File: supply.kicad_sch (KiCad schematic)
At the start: 12 parts

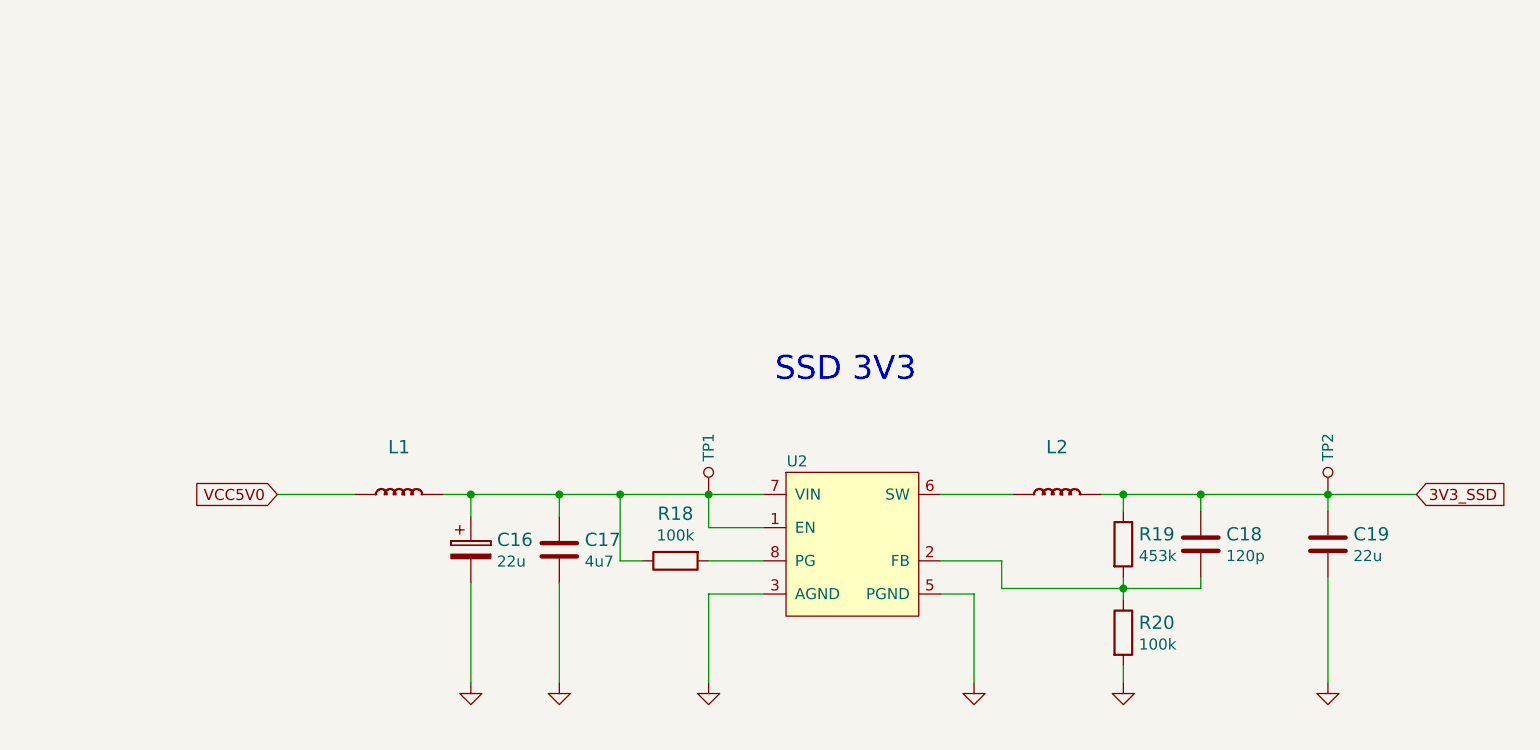
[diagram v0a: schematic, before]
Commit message: Exchanged flyback to CUI DCDC converter on schematics. Added logos.
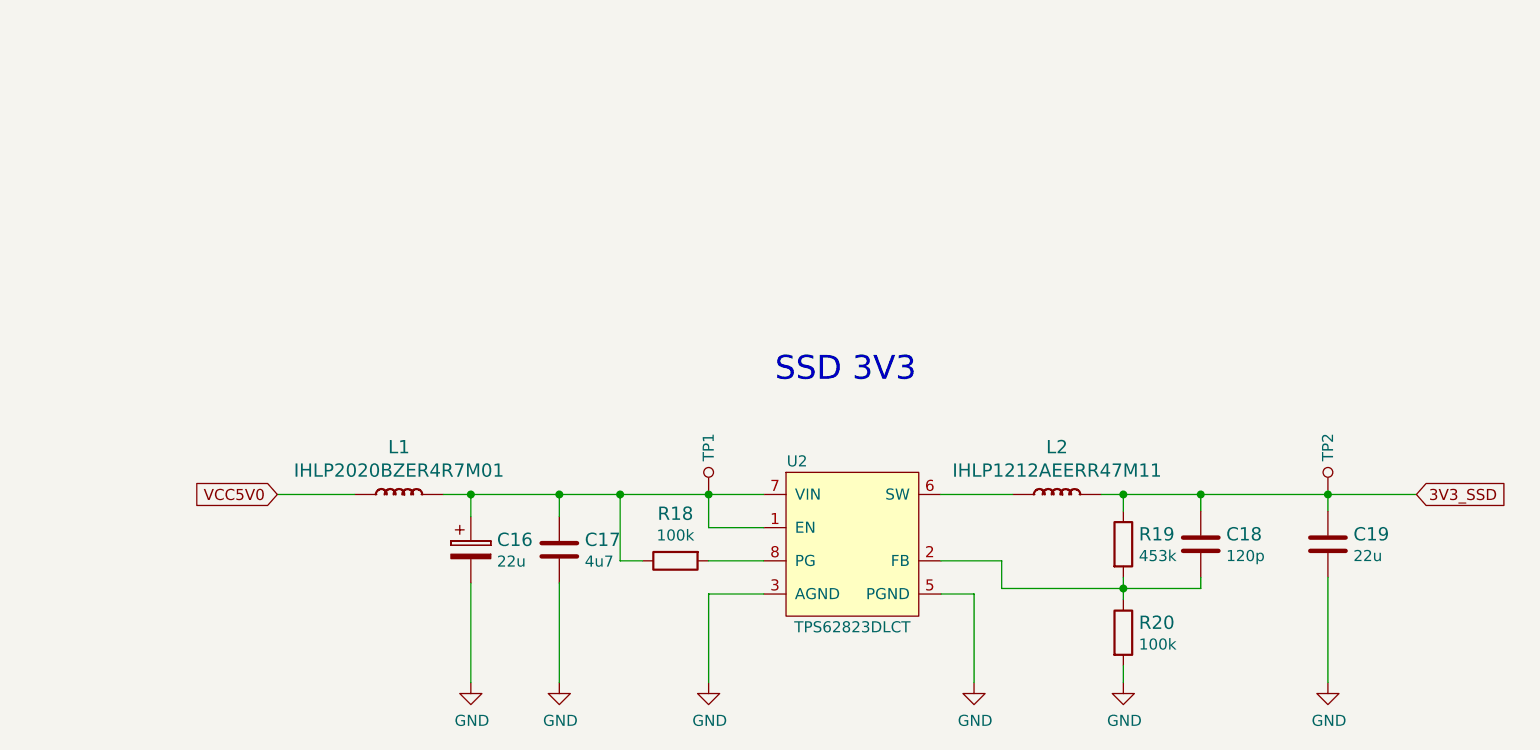
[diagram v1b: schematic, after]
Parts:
- C16: value (none) -> C_22u_KEMET_A; footprint scalenode-footprints: -> scalenode-footprints:KEMET_A
- C17: value (none) -> C_4u7_0603; footprint scalenode-footprints: -> scalenode-footprints:0603-cap
- C18: value (none) -> C_120p_0402; footprint scalenode-footprints: -> scalenode-footprints:0402-res
- C19: value (none) -> C_22u_1210; footprint scalenode-footprints: -> scalenode-footprints:1210-cap
- L1: value (none) -> IHLP2020BZER4R7M01; footprint scalenode-footprints: -> scalenode-footprints:IHLP2020BZER4R7M01
- L2: value (none) -> IHLP1212AEERR47M11; footprint scalenode-footprints: -> scalenode-footprints:IHLP-1212AE
- R18: value (none) -> R_100k_0603; footprint scalenode-footprints: -> scalenode-footprints:0603-res
- R19: value (none) -> R_453k_0402; footprint scalenode-footprints: -> scalenode-footprints:0402-res
- R20: value (none) -> R_100k_0402; footprint scalenode-footprints: -> scalenode-footprints:0402-res
- TP1, TP2: value (none) -> TP_SMD1MM; footprint scalenode-footprints: -> scalenode-footprints:Testpoint_smd_1mm
- U2: value (none) -> TPS62823DLCT; footprint scalenode-footprints: -> scalenode-footprints:QFN-8_2x1mm

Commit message: Added text fields with schematic descriptions
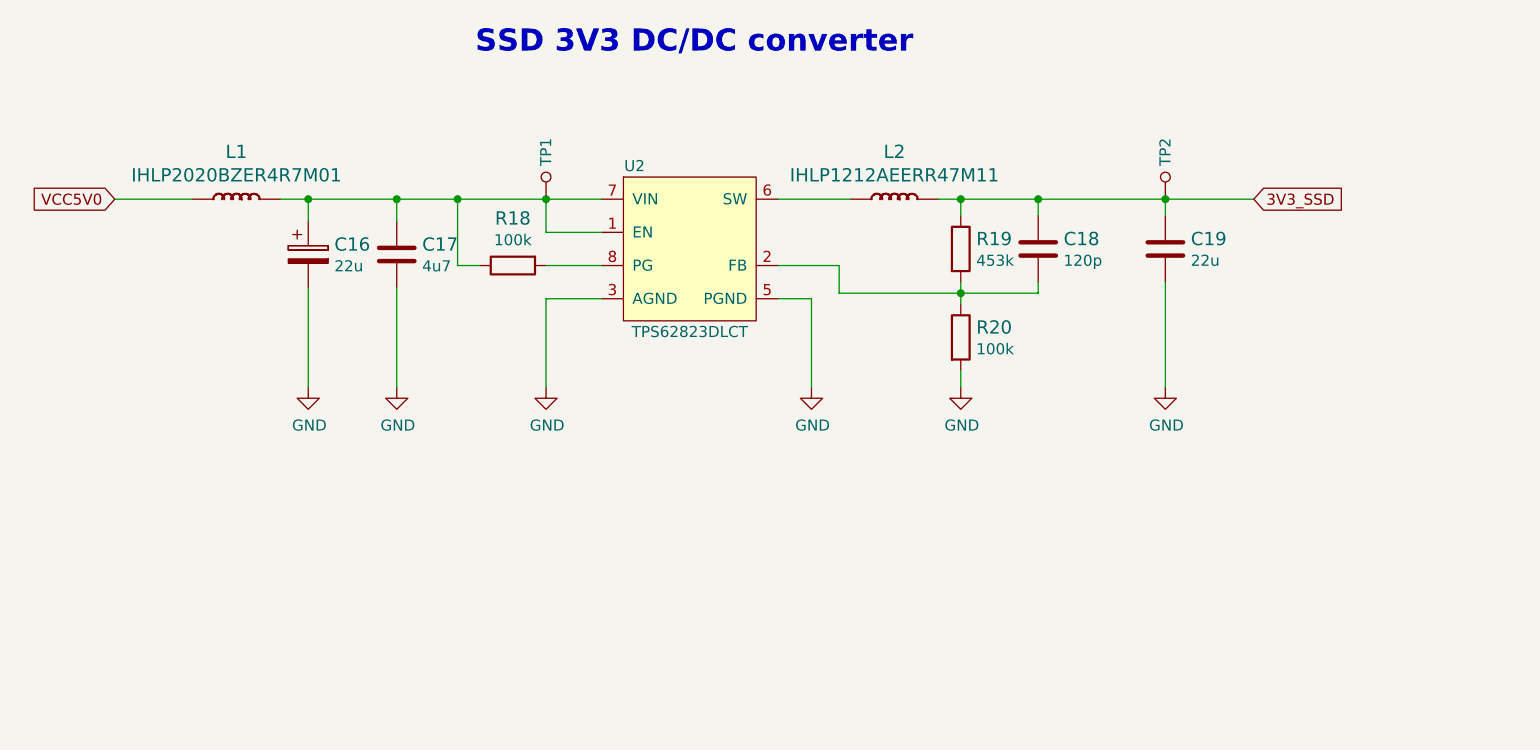
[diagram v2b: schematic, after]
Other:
- note added: "SSD 3V3 DC/DC converter"
- note removed: "SSD 3V3"
- moved on the sheet: C16, C17, C18, C19, L1, L2, R18, R19, R20, TP1, TP2, U2

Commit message: Implemented changes from rev 1.0.4. New components initial placement
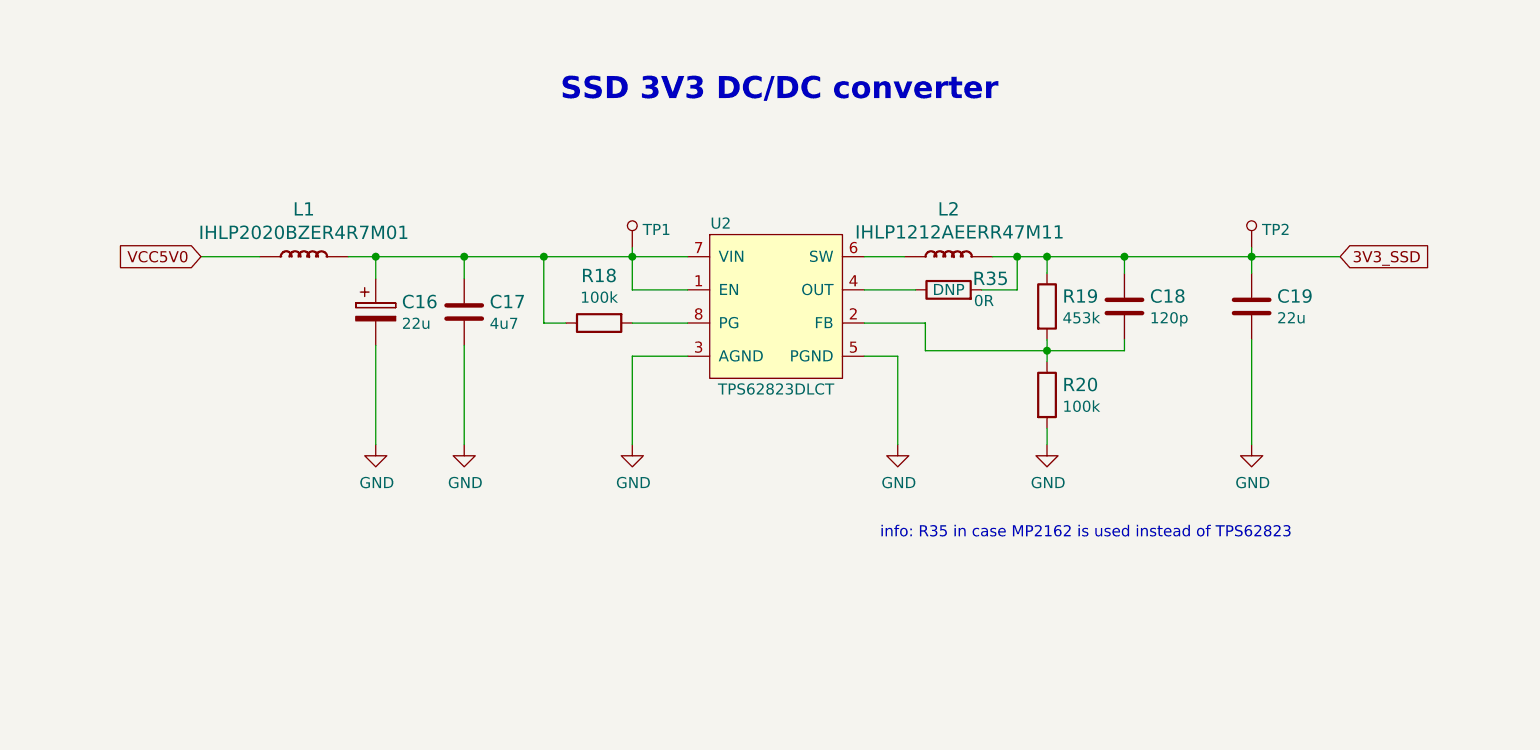
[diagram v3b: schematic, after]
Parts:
- added R35: R_0R_0402, antmicro-footprints:0402-res, symbol antmicroResistors0402:R_0R_0402
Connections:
- net 3V3_SSD: now also R35.2
- new net: R35.1, U2.4 (OUT)
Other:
- note added: "info: R35 in case MP2162 is used instead of TPS62823"
- moved on the sheet: C16, C17, C18, C19, L1, L2, R18, R19, R20, TP1, TP2

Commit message: loclib
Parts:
- R35: footprint antmicro-footprints:0402-res -> scalenode-footprints:0402-res; symbol antmicroResistors0402:R_0R_0402 -> scalenode:R_0R_0402

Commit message: Added comment on MP2162 option
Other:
- note added: "info: R35 in case MP2162 is used instead of TPS62823 info: L2 in case MP2162 is IHLP1212AEER1R5M11"
- note removed: "info: R35 in case MP2162 is used instead of TPS62823"
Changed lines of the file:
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@@
     )
   )
-  (text "info: R35 in case MP2162 is used instead of TPS62823"
-    (at 217.17 172.212 0)
+  (text "info: R35 in case MP2162 is used instead of TPS62823\ninfo: L2 in case MP2162 is IHLP1212AEER1R5M11"
+    (at 207.645 172.085 0)
     (effects (font (size 1.27 1.27)) (justify left bottom))
   )

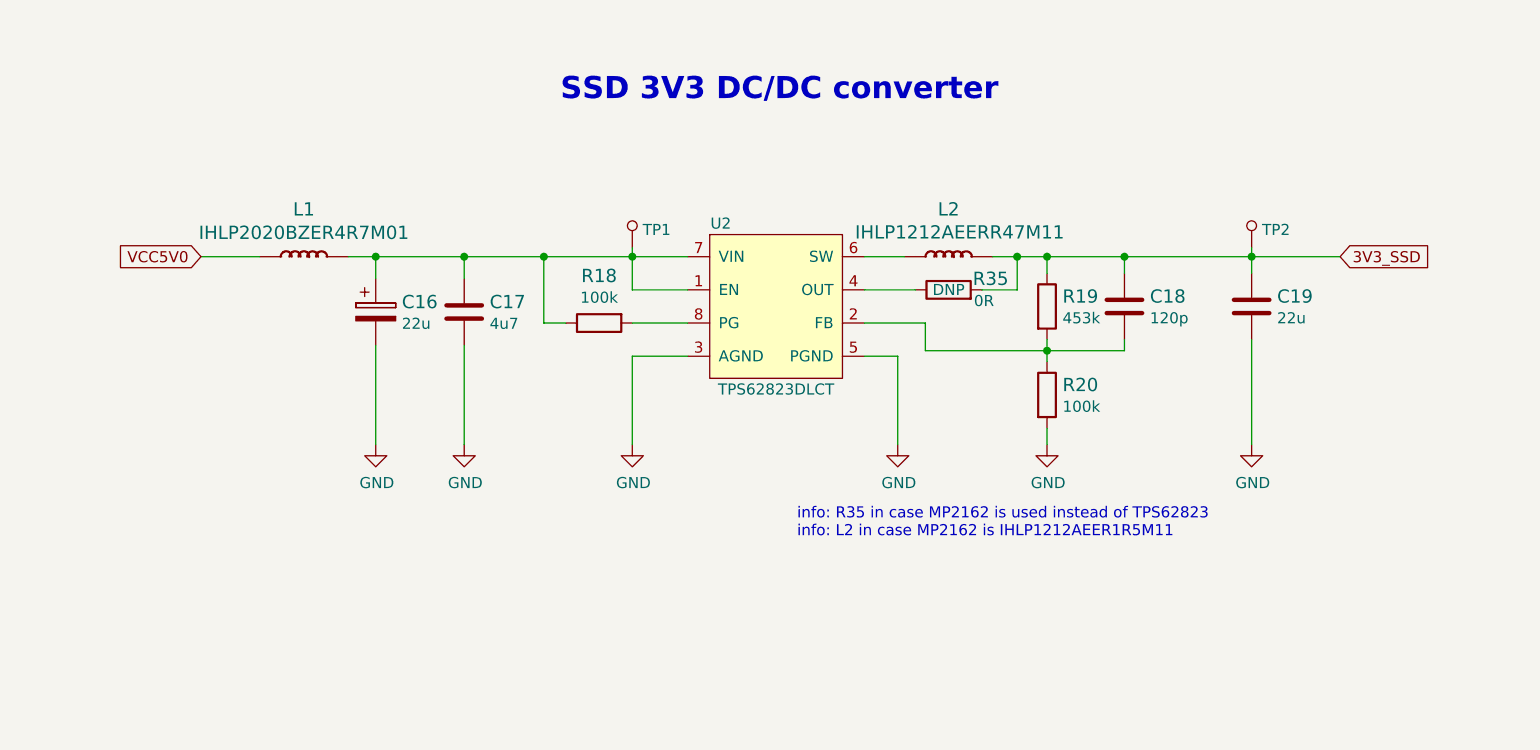
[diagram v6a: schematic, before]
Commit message: Changed 3V3 converter to AP62301WU-7
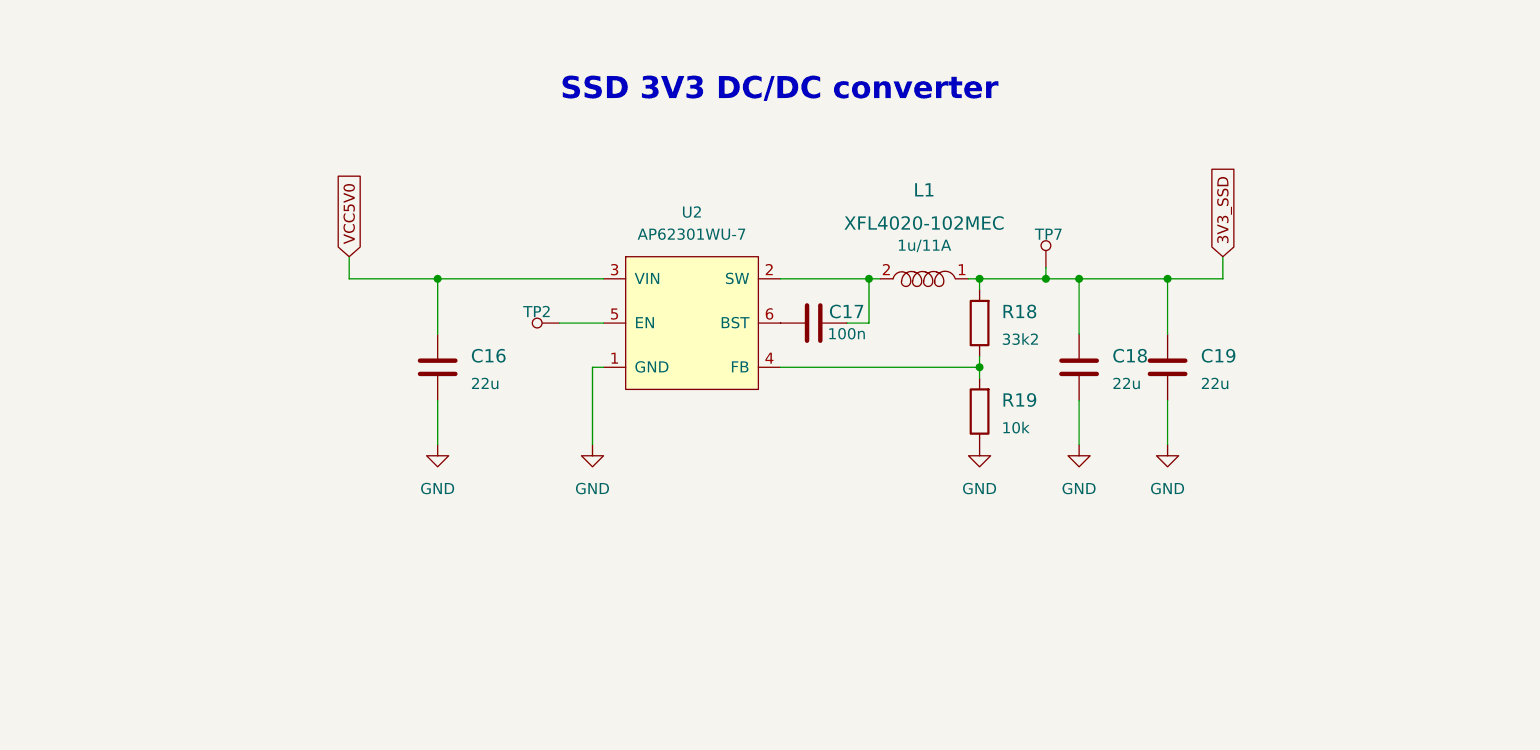
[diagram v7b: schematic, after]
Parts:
- removed C16: C_22u_KEMET_A, scalenode-footprints:KEMET_A, symbol scalenode:C_22u_KEMET_A
- removed C17: C_4u7_0603, scalenode-footprints:0603-cap, symbol scalenode:C_4u7_0603
- removed C18: C_120p_0402, scalenode-footprints:0402-res, symbol scalenode:C_120p_0402
- removed C19: C_22u_1210, scalenode-footprints:1210-cap, symbol scalenode:C_22u_1210
- removed L1: IHLP2020BZER4R7M01, scalenode-footprints:IHLP2020BZER4R7M01, symbol scalenode:IHLP2020BZER4R7M01
- removed L2: IHLP1212AEERR47M11, scalenode-footprints:IHLP-1212AE, symbol scalenode:IHLP1212AEERR47M11
- removed R18: R_100k_0603, scalenode-footprints:0603-res, symbol scalenode:R_100k_0603
- removed R19: R_453k_0402, scalenode-footprints:0402-res, symbol scalenode:R_453k_0402
- removed R20: R_100k_0402, scalenode-footprints:0402-res, symbol scalenode:R_100k_0402
- removed R35: R_0R_0402, scalenode-footprints:0402-res, symbol scalenode:R_0R_0402
- removed TP1: TP_SMD1MM, scalenode-footprints:Testpoint_smd_1mm, symbol scalenode:TP_SMD1MM
- removed U2: TPS62823DLCT, scalenode-footprints:QFN-8_2x1mm, symbol scalenode:TPS62823DLCT
- added C16, C18, C19: C_22u_0805_10V, antmicro-footprints:0805-cap, symbol antmicroCapacitorsmisc:C_22u_0805_10V
- added C17: C_100n_0402, antmicro-footprints:0402-cap, symbol antmicroCapacitors0402:C_100n_0402
- added L1: XFL4020-102MEC, antmicro-footprints:XFL4020-102MEB, symbol antmicroFixedInductors:XFL4020-102MEC
- added R18: R_33k2_0402, antmicro-footprints:0402-res, symbol antmicroResistors0402:R_33k2_0402
- added R19: R_10k_0402, antmicro-footprints:0402-res, symbol antmicroResistors0402:R_10k_0402
- added TP7: TP_SMD1MM, scalenode-footprints:Testpoint_smd_1mm, symbol scalenode:TP_SMD1MM
- added U2: AP62301WU-7, antmicro-footprints:TSOT23-6, symbol antmicroDCDCConverters:AP62301WU-7
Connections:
- net 3V3_SSD: now also C18.1, C19.1, L1.1, R18.2, TP7.1; no longer TP2.1
- net GND: now also C16.2, C18.2, C19.2, R19.1, U2.1 (GND)
- net VCC5V0: now also C16.1, U2.3 (VIN)
- new net: C17.2, L1.2, U2.2 (SW)
- new net: R18.1, R19.2, U2.4 (FB)
- new net: TP2.1, U2.5 (EN)
- new net: C17.1, U2.6 (BST)
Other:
- note removed: "info: R35 in case MP2162 is used instead of TPS62823 info: L2 in case MP2162 is IHLP1212AEER1R5M11"
